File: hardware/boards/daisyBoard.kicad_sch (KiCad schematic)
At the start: 113 parts, among them IC1 TL072, IC2 TL072, IC3 TL072, IC4 TL072, J1 LEFT Pin ROW, J10 AudioJack_OUT_2, J11 AudioJack_OUT_2, J13 LEFT Pin ROW Daisy, J14 RIGHT Pin ROW DAISY, J15 Daisy Pin Breakout LEFT, J16 Daisy PIN Breakout RIGHT, J2 RIGHT Pin Row, J3 ESP32 Pin Breakout RIGHT, J4 ESP32 Pin Breakout LEFT, J6 AudioJack3, J7 AudioJack3, J8 AudioJack_IN_1, J9 AudioJack_IN_2, U1 MCP6002-xSN, U2 MCP6002-xSN, U3 MCP6002-xSN

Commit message: added some changes and checks adnd did a review
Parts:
- C18, C26, C27, C28, C29, C30, C31: footprint (none) -> Capacitor_SMD:C_1206_3216Metric
- C32: renamed from 100nF1; value C26 -> 100nF
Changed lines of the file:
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@@
 			)
 		)
-		(property "Footprint" ""
+		(property "Footprint" "Capacitor_SMD:C_1206_3216Metric"
 			(at 493.0648 223.52 0)
 			(hide yes)
@@
 			)
 		)
-		(property "Footprint" ""
+		(property "Footprint" "Capacitor_SMD:C_1206_3216Metric"
 			(at 127.3048 97.79 0)
 			(hide yes)
@@
 			)
 		)
-		(property "Footprint" ""
+		(property "Footprint" "Capacitor_SMD:C_1206_3216Metric"
 			(at 197.1548 106.68 0)
 			(hide yes)
@@
 			)
 		)
-		(property "Footprint" ""
+		(property "Footprint" "Capacitor_SMD:C_1206_3216Metric"
 			(at 120.3452 30.48 0)
 			(hide yes)
@@
 		(in_pos_files yes)
 		(dnp no)
-		(property "Reference" "100nF1"
+		(property "Reference" "C32"
 			(at 423.164 45.72 90)
 			(show_name no)
@@
 			)
 		)
-		(property "Value" "C26"
+		(property "Value" "100nF"
 			(at 426.72 42.926 90)
 			(show_name no)
@@
 			(project "daisyBoard"
 				(path "/f52c2822-383d-4296-bc07-76547c2833aa"
-					(reference "100nF1")
+					(reference "C32")
 					(unit 1)
 				)
@@
 			)
 		)
-		(property "Footprint" ""
+		(property "Footprint" "Capacitor_SMD:C_1206_3216Metric"
 			(at 385.1148 91.44 0)
 			(hide yes)
@@
 			)
 		)
-		(property "Footprint" ""
+		(property "Footprint" "Capacitor_SMD:C_1206_3216Metric"
 			(at 205.4352 24.13 0)
 			(hide yes)
@@
 			)
 		)
-		(property "Footprint" ""
+		(property "Footprint" "Capacitor_SMD:C_1206_3216Metric"
 			(at 517.8552 93.98 0)
 			(hide yes)

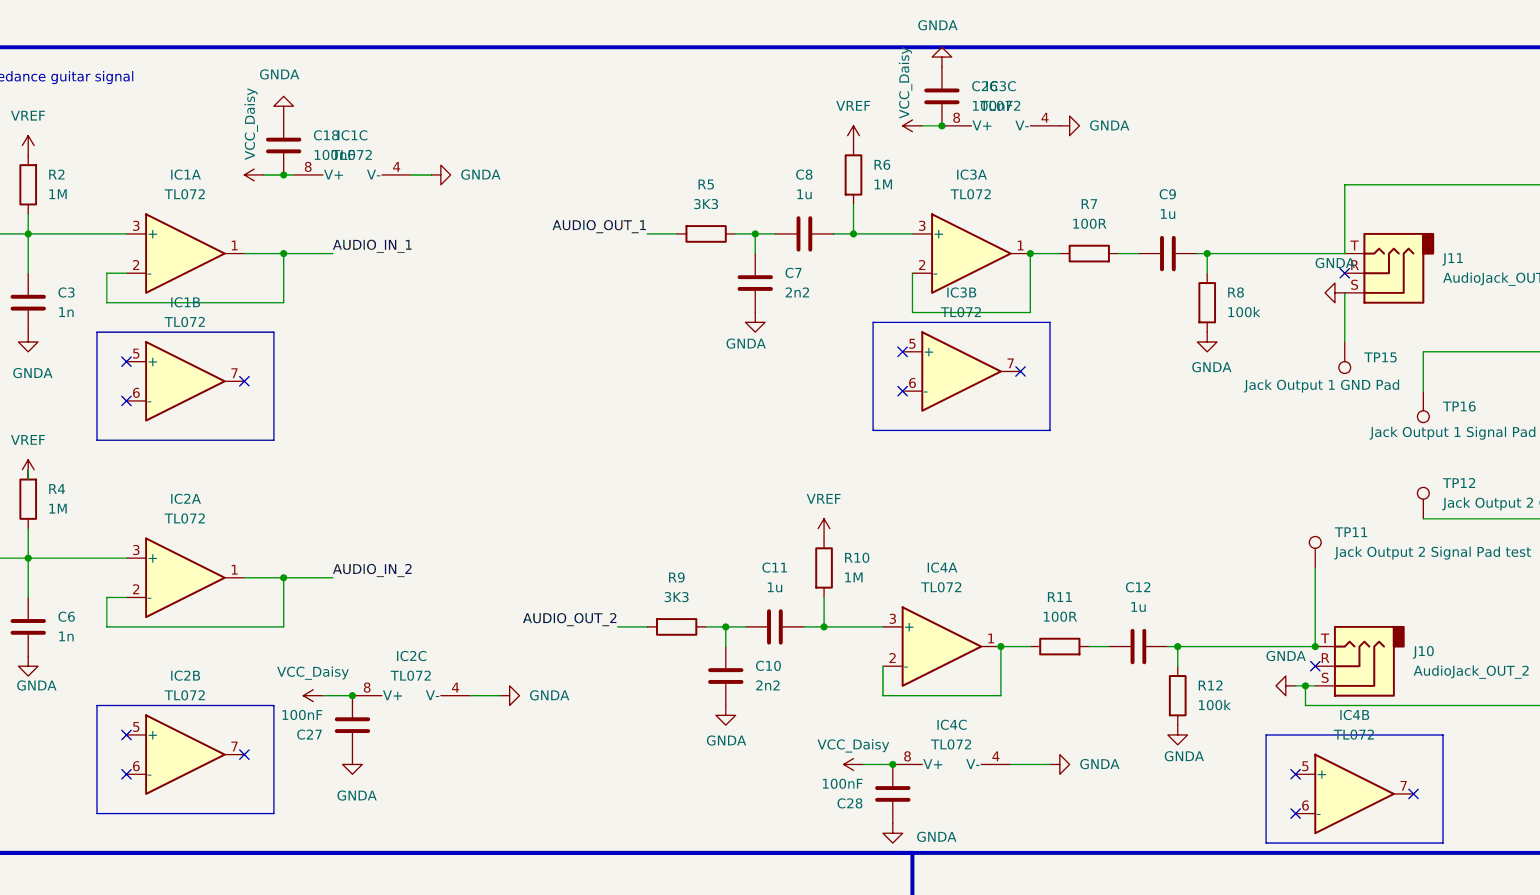
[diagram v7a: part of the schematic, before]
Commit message: updated TL072 to the H model in order to account ofr the 5V in that is currently lower than the 7V TL072 operating range
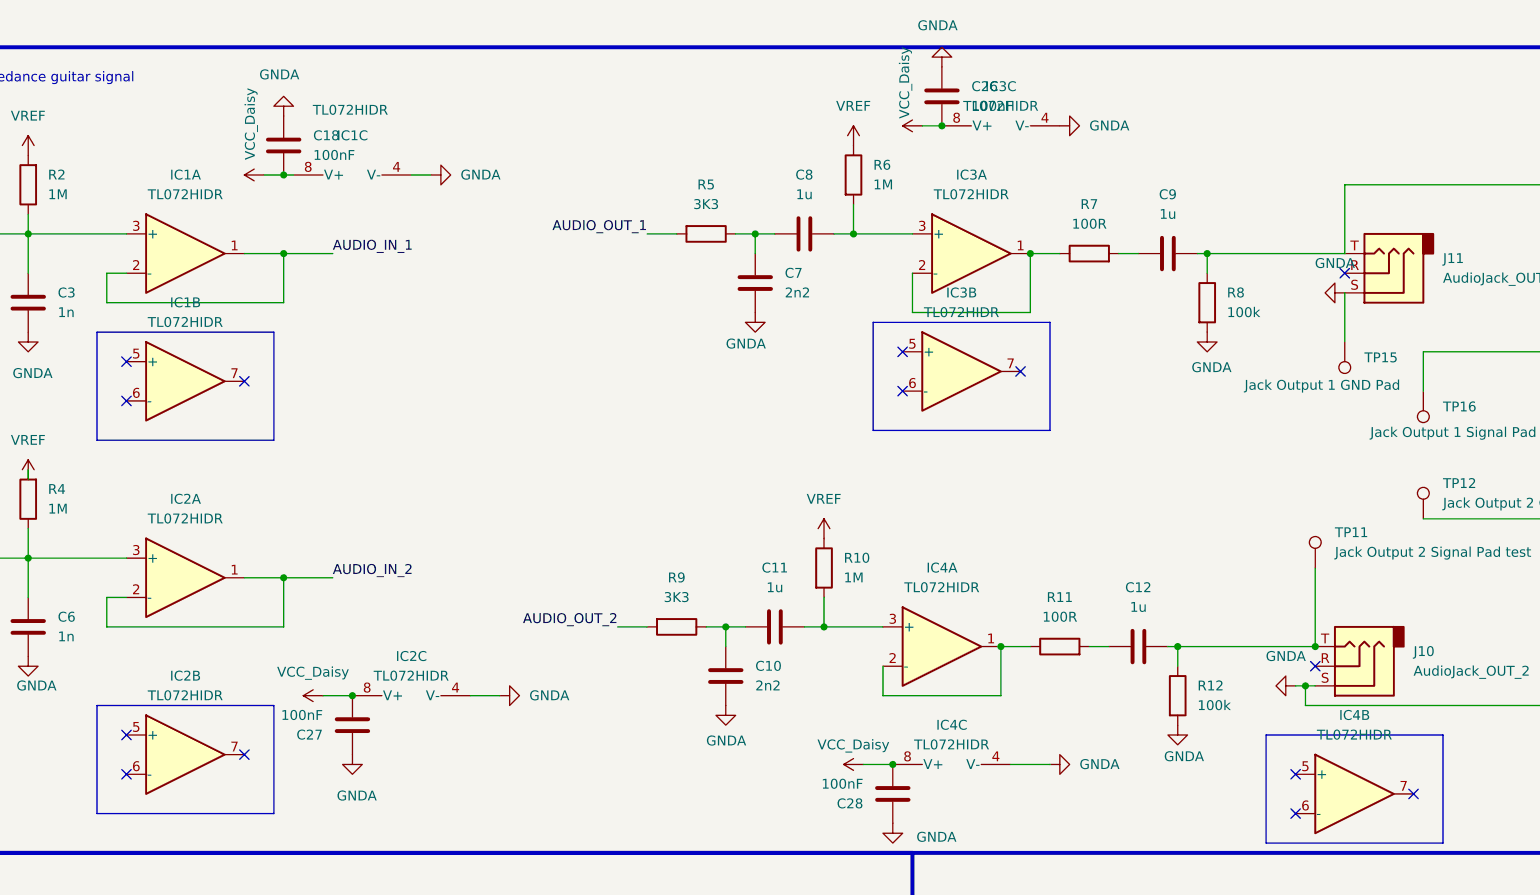
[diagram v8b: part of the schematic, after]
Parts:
- IC1, IC2, IC3, IC4: value TL072 -> TL072HIDR
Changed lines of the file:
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@@
 			)
 		)
-		(property "Value" "TL072"
+		(property "Value" "TL072HIDR"
 			(at 135.89 95.25 90)
 			(show_name no)
@@
 			)
 		)
-		(property "Datasheet" "http://www.ti.com/lit/ds/symlink/tl071.pdf"
+		(property "Datasheet" "https://www.ti.com/cn/lit/gpn/tl074a"
 			(at 135.89 95.25 0)
 			(hide yes)
@@
 		(in_pos_files yes)
 		(dnp no)
-		(fields_autoplaced yes)
 		(property "Reference" "IC1"
 			(at 128.27 25.4 90)
@@
 			)
 		)
-		(property "Value" "TL072"
-			(at 128.27 27.94 90)
+		(property "Value" "TL072HIDR"
+			(at 128.016 22.098 90)
 			(show_name no)
 			(do_not_autoplace no)
@@
 			)
 		)
-		(property "Datasheet" "http://www.ti.com/lit/ds/symlink/tl071.pdf"
+		(property "Datasheet" "https://www.ti.com/cn/lit/gpn/tl074a"
 			(at 128.27 27.94 0)
 			(hide yes)
@@
 			)
 		)
-		(property "Value" "TL072"
+		(property "Value" "TL072HIDR"
 			(at 207.01 48.26 0)
 			(show_name no)
@@
 			)
 		)
-		(property "Datasheet" "http://www.ti.com/lit/ds/symlink/tl071.pdf"
+		(property "Datasheet" "https://www.ti.com/cn/lit/gpn/tl074a"
 			(at 207.01 55.88 0)
 			(hide yes)
@@
 			)
 		)
-		(property "Value" "TL072"
+		(property "Value" "TL072HIDR"
 			(at 106.68 74.93 0)
 			(show_name no)
@@
 			)
 		)
-		(property "Datasheet" "http://www.ti.com/lit/ds/symlink/tl071.pdf"
+		(property "Datasheet" "https://www.ti.com/cn/lit/gpn/tl074a"
 			(at 106.68 82.55 0)
 			(hide yes)
@@
 			)
 		)
-		(property "Value" "TL072"
+		(property "Value" "TL072HIDR"
 			(at 106.68 49.53 0)
 			(show_name no)
@@
 			)
 		)
-		(property "Datasheet" "http://www.ti.com/lit/ds/symlink/tl071.pdf"
+		(property "Datasheet" "https://www.ti.com/cn/lit/gpn/tl074a"
 			(at 106.68 57.15 0)
 			(hide yes)
@@
 			)
 		)
-		(property "Value" "TL072"
+		(property "Value" "TL072HIDR"
 			(at 212.09 21.59 90)
 			(show_name no)
@@
 			)
 		)
-		(property "Datasheet" "http://www.ti.com/lit/ds/symlink/tl071.pdf"
+		(property "Datasheet" "https://www.ti.com/cn/lit/gpn/tl074a"
 			(at 212.09 21.59 0)
 			(hide yes)
@@
 			)
 		)
-		(property "Value" "TL072"
+		(property "Value" "TL072HIDR"
 			(at 204.47 83.82 0)
 			(show_name no)
@@
 			)
 		)
-		(property "Datasheet" "http://www.ti.com/lit/ds/symlink/tl071.pdf"
+		(property "Datasheet" "https://www.ti.com/cn/lit/gpn/tl074a"
 			(at 204.47 91.44 0)
 			(hide yes)
@@
 			)
 		)
-		(property "Value" "TL072"
+		(property "Value" "TL072HIDR"
 			(at 205.74 104.14 90)
 			(show_name no)
@@
 			)
 		)
-		(property "Datasheet" "http://www.ti.com/lit/ds/symlink/tl071.pdf"
+		(property "Datasheet" "https://www.ti.com/cn/lit/gpn/tl074a"
 			(at 205.74 104.14 0)
 			(hide yes)
@@
 			)
 		)
-		(property "Value" "TL072"
+		(property "Value" "TL072HIDR"
 			(at 257.81 102.87 0)
 			(show_name no)
@@
 			)
 		)
-		(property "Datasheet" "http://www.ti.com/lit/ds/symlink/tl071.pdf"
+		(property "Datasheet" "https://www.ti.com/cn/lit/gpn/tl074a"
 			(at 257.81 110.49 0)
 			(hide yes)
@@
 			)
 		)
-		(property "Value" "TL072"
+		(property "Value" "TL072HIDR"
 			(at 106.68 97.79 0)
 			(show_name no)
@@
 			)
 		)
-		(property "Datasheet" "http://www.ti.com/lit/ds/symlink/tl071.pdf"
+		(property "Datasheet" "https://www.ti.com/cn/lit/gpn/tl074a"
 			(at 106.68 105.41 0)
 			(hide yes)
@@
 			)
 		)
-		(property "Value" "TL072"
+		(property "Value" "TL072HIDR"
 			(at 106.68 33.02 0)
 			(show_name no)
@@
 			)
 		)
-		(property "Datasheet" "http://www.ti.com/lit/ds/symlink/tl071.pdf"
+		(property "Datasheet" "https://www.ti.com/cn/lit/gpn/tl074a"
 			(at 106.68 40.64 0)
 			(hide yes)
@@
 			)
 		)
-		(property "Value" "TL072"
+		(property "Value" "TL072HIDR"
 			(at 208.28 33.02 0)
 			(show_name no)
@@
 			)
 		)
-		(property "Datasheet" "http://www.ti.com/lit/ds/symlink/tl071.pdf"
+		(property "Datasheet" "https://www.ti.com/cn/lit/gpn/tl074a"
 			(at 208.28 40.64 0)
 			(hide yes)
